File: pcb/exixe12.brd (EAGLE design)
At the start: 20 x 40 mm, 42 parts

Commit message: clened up added credit
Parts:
- N1: device 0-nixies-russian:IN-12 -> exixe12:IN-12
- moved R4 0.25 mm to (6.54, 25.9)
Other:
- board text added: "dekuNukem"
- board text added: "exixe12"
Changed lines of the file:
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@@
 <layers>
 <layer number="1" name="Top" color="4" fill="1" visible="yes" active="yes"/>
-<layer number="2" name="Route2" color="1" fill="3" visible="no" active="yes"/>
-<layer number="3" name="Route3" color="4" fill="3" visible="no" active="yes"/>
-<layer number="4" name="Route4" color="1" fill="4" visible="no" active="yes"/>
-<layer number="5" name="Route5" color="4" fill="4" visible="no" active="yes"/>
-<layer number="6" name="Route6" color="1" fill="8" visible="no" active="yes"/>
-<layer number="7" name="Route7" color="4" fill="8" visible="no" active="yes"/>
-<layer number="8" name="Route8" color="1" fill="2" visible="no" active="yes"/>
-<layer number="9" name="Route9" color="4" fill="2" visible="no" active="yes"/>
-<layer number="10" name="Route10" color="1" fill="7" visible="no" active="yes"/>
-<layer number="11" name="Route11" color="4" fill="7" visible="no" active="yes"/>
-<layer number="12" name="Route12" color="1" fill="5" visible="no" active="yes"/>
-<layer number="13" name="Route13" color="4" fill="5" visible="no" active="yes"/>
-<layer number="14" name="Route14" color="1" fill="6" visible="no" active="yes"/>
-<layer number="15" name="Route15" color="4" fill="6" visible="no" active="yes"/>
+<layer number="2" name="Route2" color="1" fill="3" visible="yes" active="yes"/>
+<layer number="3" name="Route3" color="4" fill="3" visible="yes" active="yes"/>
+<layer number="4" name="Route4" color="1" fill="4" visible="yes" active="yes"/>
+<layer number="5" name="Route5" color="4" fill="4" visible="yes" active="yes"/>
+<layer number="6" name="Route6" color="1" fill="8" visible="yes" active="yes"/>
+<layer number="7" name="Route7" color="4" fill="8" visible="yes" active="yes"/>
+<layer number="8" name="Route8" color="1" fill="2" visible="yes" active="yes"/>
+<layer number="9" name="Route9" color="4" fill="2" visible="yes" active="yes"/>
+<layer number="10" name="Route10" color="1" fill="7" visible="yes" active="yes"/>
+<layer number="11" name="Route11" color="4" fill="7" visible="yes" active="yes"/>
+<layer number="12" name="Route12" color="1" fill="5" visible="yes" active="yes"/>
+<layer number="13" name="Route13" color="4" fill="5" visible="yes" active="yes"/>
+<layer number="14" name="Route14" color="1" fill="6" visible="yes" active="yes"/>
+<layer number="15" name="Route15" color="4" fill="6" visible="yes" active="yes"/>
 <layer number="16" name="Bottom" color="1" fill="1" visible="yes" active="yes"/>
 <layer number="17" name="Pads" color="2" fill="1" visible="yes" active="yes"/>
@@
 <layer number="37" name="tTest" color="7" fill="1" visible="no" active="yes"/>
 <layer number="38" name="bTest" color="7" fill="1" visible="no" active="yes"/>
-<layer number="39" name="tKeepout" color="4" fill="11" visible="no" active="yes"/>
-<layer number="40" name="bKeepout" color="1" fill="11" visible="no" active="yes"/>
-<layer number="41" name="tRestrict" color="4" fill="10" visible="no" active="yes"/>
-<layer number="42" name="bRestrict" color="1" fill="10" visible="no" active="yes"/>
+<layer number="39" name="tKeepout" color="4" fill="11" visible="yes" active="yes"/>
+<layer number="40" name="bKeepout" color="1" fill="11" visible="yes" active="yes"/>
+<layer number="41" name="tRestrict" color="4" fill="10" visible="yes" active="yes"/>
+<layer number="42" name="bRestrict" color="1" fill="10" visible="yes" active="yes"/>
 <layer number="43" name="vRestrict" color="2" fill="10" visible="no" active="yes"/>
-<layer number="44" name="Drills" color="7" fill="1" visible="no" active="yes"/>
-<layer number="45" name="Holes" color="7" fill="1" visible="no" active="yes"/>
+<layer number="44" name="Drills" color="7" fill="1" visible="yes" active="yes"/>
+<layer number="45" name="Holes" color="7" fill="1" visible="yes" active="yes"/>
 <layer number="46" name="Milling" color="3" fill="1" visible="no" active="yes"/>
 <layer number="47" name="Measures" color="7" fill="1" visible="no" active="yes"/>
@@
 <text x="14.224" y="3.556" size="0.8128" layer="25" font="vector">DIO</text>
 <text x="16.637" y="3.556" size="0.8128" layer="25" font="vector">CLK</text>
-<text x="15.4178" y="35.3314" size="1.143" layer="26" font="vector" rot="MR0">G</text>
+<text x="15.4686" y="35.3314" size="1.143" layer="26" font="vector" rot="MR0">G</text>
 <text x="11.6078" y="32.639" size="1.143" layer="25" font="vector">+</text>
 <polygon width="0.1524" layer="41">
@@
 <vertex x="14.5796" y="20.0152"/>
 <vertex x="13.4112" y="19.812"/>
-<vertex x="9.144" y="24.2316"/>
-<vertex x="9.652" y="29.0576"/>
-<vertex x="9.6012" y="33.02"/>
-<vertex x="8.1788" y="36.6268"/>
+<vertex x="8.0264" y="25.2984"/>
+<vertex x="9.5504" y="29.1592"/>
+<vertex x="9.398" y="33.0708"/>
+<vertex x="8.0264" y="36.6268"/>
 <vertex x="7.2644" y="36.3728"/>
 <vertex x="7.366" y="36.068"/>
 </polygon>
+<text x="10.414" y="14.224" size="1.27" layer="26" font="vector" rot="MR0">exixe12</text>
+<text x="10.414" y="11.176" size="1.27" layer="26" font="vector" rot="MR0">dekuNukem</text>
 </plain>
 <attributes>
@@
 <attribute name="VALUE" x="7.909" y="27.88" size="1.016" layer="27"/>
 </element>
-<element name="R4" library="joyAnalog" package="0805" value="4K7" x="6.7458" y="26.0106" smashed="yes" rot="R90">
-<attribute name="NAME" x="4.9032" y="23.6453" size="0.8128" layer="25" font="vector"/>
+<element name="R4" library="joyAnalog" package="0805" value="4K7" x="6.5426" y="25.8582" smashed="yes" rot="R90">
+<attribute name="NAME" x="4.7" y="23.4929" size="0.8128" layer="25" font="vector"/>
 </element>
 <element name="Q5" library="nixx" package="SOT323" value="" x="3.175" y="33.909" smashed="yes">
@@
 <attribute name="NAME" x="12.4968" y="14.7193" size="0.8128" layer="25" font="vector"/>
 </element>
-<element name="N1" library="0-nixies-russian" package="IN-12" value="IN-12B" x="10.4" y="26.3" smashed="yes"/>
+<element name="N1" library="exixe12" package="IN-12" value="IN-12B" x="10.4" y="26.3" smashed="yes"/>
 <element name="R19" library="joyAnalog" package="0805" value="68K" x="6.858" y="38.989" smashed="yes" rot="R180">
 <attribute name="NAME" x="8.8519" y="38.1508" size="0.6096" layer="25" rot="R90"/>
@@
 <wire x1="9.8044" y1="23.114" x2="9.4996" y2="23.4188" width="0.2032" layer="1"/>
 <wire x1="9.4996" y1="23.4188" x2="8.7376" y2="23.4188" width="0.2032" layer="1"/>
-<wire x1="8.7376" y1="23.4188" x2="7.7216" y2="24.4348" width="0.2032" layer="1"/>
-<wire x1="7.7216" y1="24.4348" x2="7.7216" y2="27.432" width="0.2032" layer="1"/>
-<wire x1="7.7216" y1="27.432" x2="7.334" y2="27.8196" width="0.2032" layer="1"/>
-<wire x1="7.334" y1="27.8196" x2="7.334" y2="28.31" width="0.1524" layer="1"/>
 <wire x1="3.825" y1="33.009" x2="2.6675625" y2="31.8515625" width="0.2032" layer="1"/>
 <wire x1="2.6675625" y1="31.8515625" x2="2.6675625" y2="28.702" width="0.2032" layer="1"/>
 <wire x1="15.08" y1="38.2" x2="9.256" y2="38.2" width="0.254" layer="1"/>
 <wire x1="9.256" y1="38.2" x2="9.256" y2="39.127" width="0.254" layer="1"/>
+<wire x1="8.7376" y1="23.4188" x2="7.62" y2="24.5364" width="0.2032" layer="1"/>
+<wire x1="7.62" y1="28.024" x2="7.334" y2="28.31" width="0.2032" layer="1"/>
+<wire x1="7.62" y1="24.5364" x2="7.62" y2="28.024" width="0.2032" layer="1"/>
 </signal>
 <signal name="N$1">
@@
 <contactref element="Q4" pad="1"/>
 <contactref element="R4" pad="2"/>
-<wire x1="6.034" y1="28.31" x2="6.034" y2="27.6224" width="0.1524" layer="1"/>
-<wire x1="6.034" y1="27.6224" x2="6.7458" y2="26.9106" width="0.1524" layer="1"/>
+<wire x1="6.034" y1="28.31" x2="6.034" y2="27.2668" width="0.1524" layer="1"/>
+<wire x1="6.034" y1="27.2668" x2="6.5426" y2="26.7582" width="0.1524" layer="1"/>
 </signal>
 <signal name="N$7">
@@
 <wire x1="6.096" y1="14.732" x2="6.4516" y2="15.0876" width="0.1524" layer="1"/>
 <wire x1="6.4516" y1="15.0876" x2="6.4516" y2="16.2052" width="0.1524" layer="1"/>
-<wire x1="6.9596" y1="21.8948" x2="6.9596" y2="24.8968" width="0.1524" layer="1"/>
-<wire x1="6.9596" y1="24.8968" x2="6.7458" y2="25.1106" width="0.1524" layer="1"/>
+<wire x1="6.9596" y1="21.8948" x2="6.9596" y2="24.5412" width="0.1524" layer="1"/>
+<wire x1="6.9596" y1="24.5412" x2="6.5426" y2="24.9582" width="0.1524" layer="1"/>
 </signal>
 <signal name="STM_3">

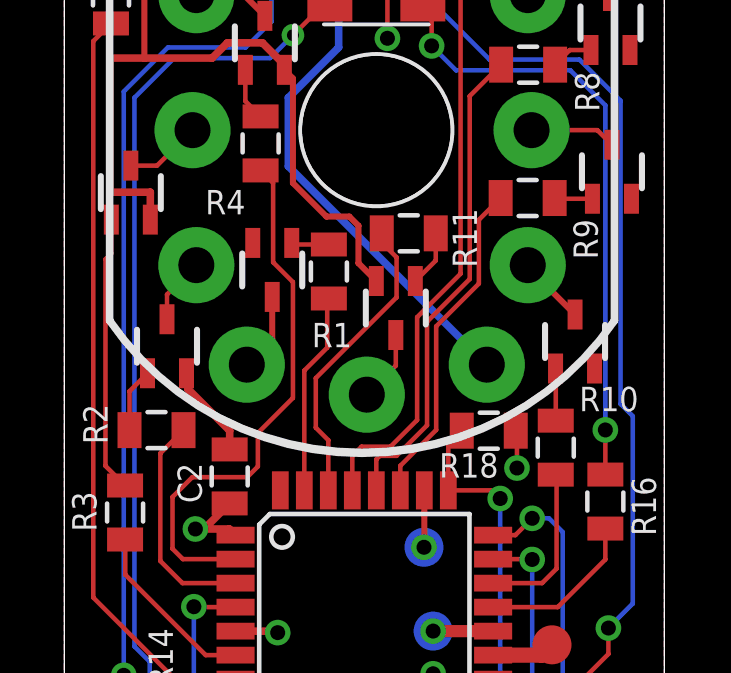
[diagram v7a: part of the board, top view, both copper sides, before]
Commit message: added nixie dot current limit resistor
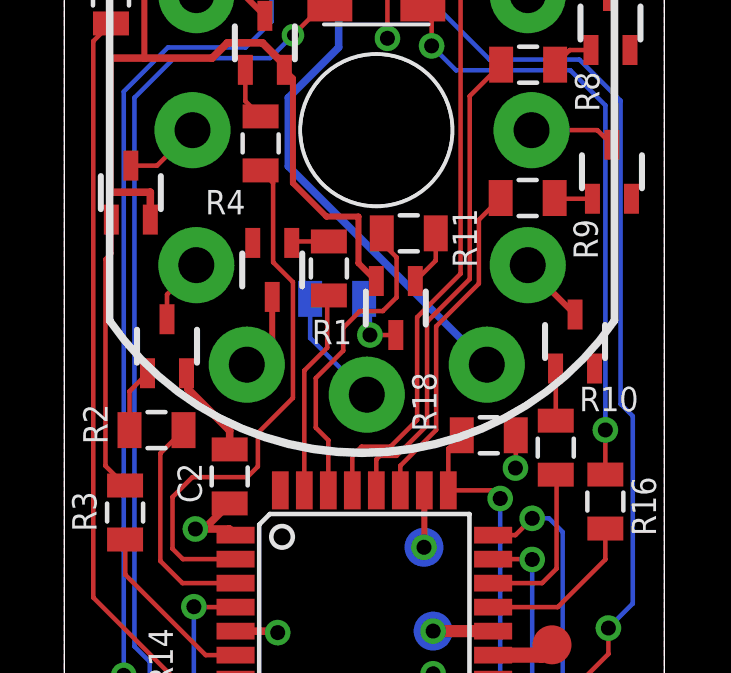
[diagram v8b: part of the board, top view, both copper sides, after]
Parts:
- added R12: 47K, joyAnalog:0805
- moved R18 0.15 mm to (14.1, 16.1)
- moved R1 0.10 mm to (8.82, 21.7)
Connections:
- new net N$22: Q11.3, R12.1
- net NIXIE_DOT_LEFT: now also R12.2; no longer Q11.3
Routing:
- net N$22: track 0.00 -> 2.26 mm, vias 0 -> 1
- net NIXIE_DOT_LEFT: track 2.39 -> 3.98 mm
